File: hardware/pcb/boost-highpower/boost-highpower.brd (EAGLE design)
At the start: 41.1 x 22.3 mm, 28 parts

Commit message: moved some components
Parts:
- moved R11 50.8 mm to (41.9, 8.89)
- moved R15 50.8 mm to (27.9, 2.54), turned to 270 degrees
- moved U$9 39.9 mm to (48.3, 11.4), turned to 270 degrees
- moved C26 37.2 mm to (26.8, 4.70), turned to 180 degrees
- moved U$10 33.4 mm to (48.3, 17.8), turned to 270 degrees
- moved C14 31.9 mm to (41.9, 11.4)
- moved R12 30.2 mm to (41.9, 10.2)
- moved U$3 27.9 mm to (38.1, 19.1)
- moved X2 22.2 mm to (64.8, 15.2)
- moved C23 21.0 mm to (59.7, 10.2)
- moved R14 20.3 mm to (25.4, 2.54), turned to 270 degrees
- moved RSENSE 18.9 mm to (27.9, 16.5), turned to 90 degrees
- moved X1 17.3 mm to (12.7, 15.2)
- moved C28 13.5 mm to (17.8, 10.2)
- moved C24 12.6 mm to (54.6, 10.2)
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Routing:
- added copper zone on layer 16, net GND
- added copper zone on layer 1, net VIN
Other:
- board size 41.1 x 22.3 mm -> 94.5 x 38.8 mm

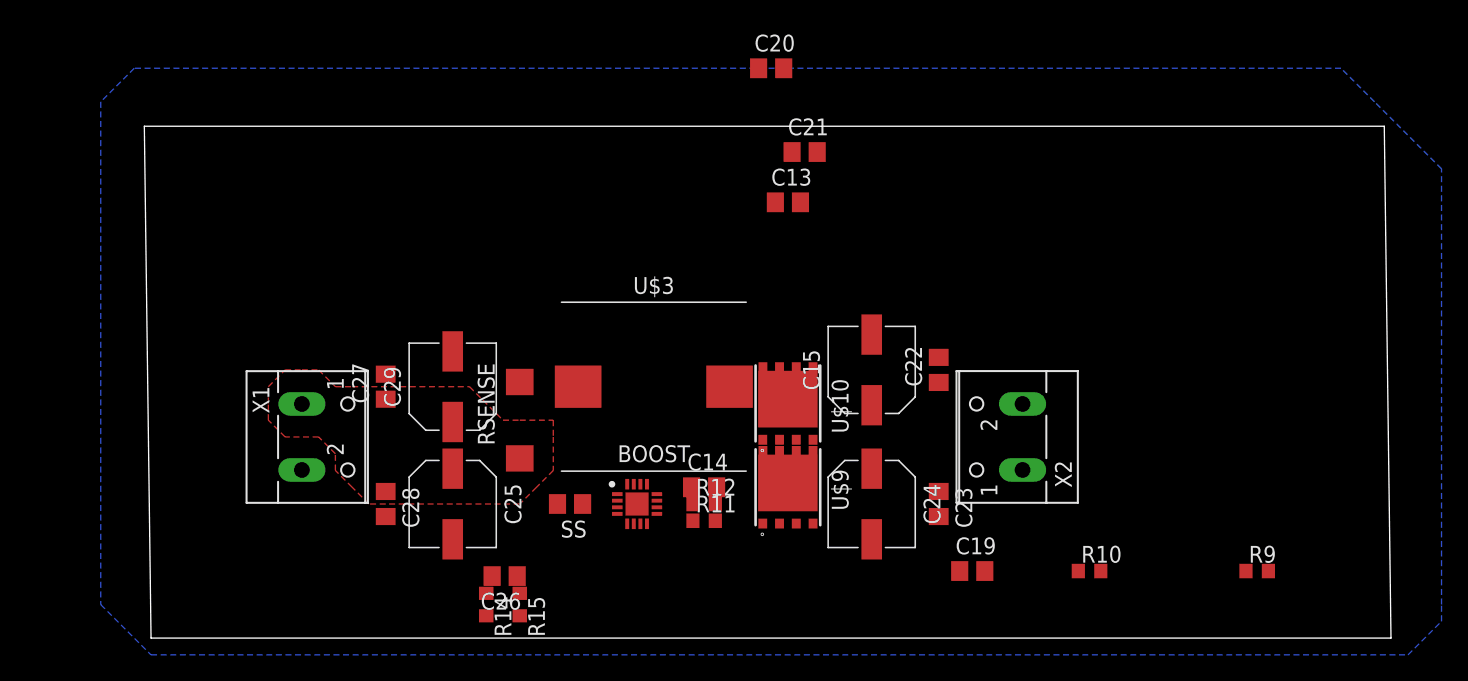
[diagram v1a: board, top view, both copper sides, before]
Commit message: Moved components to a first place
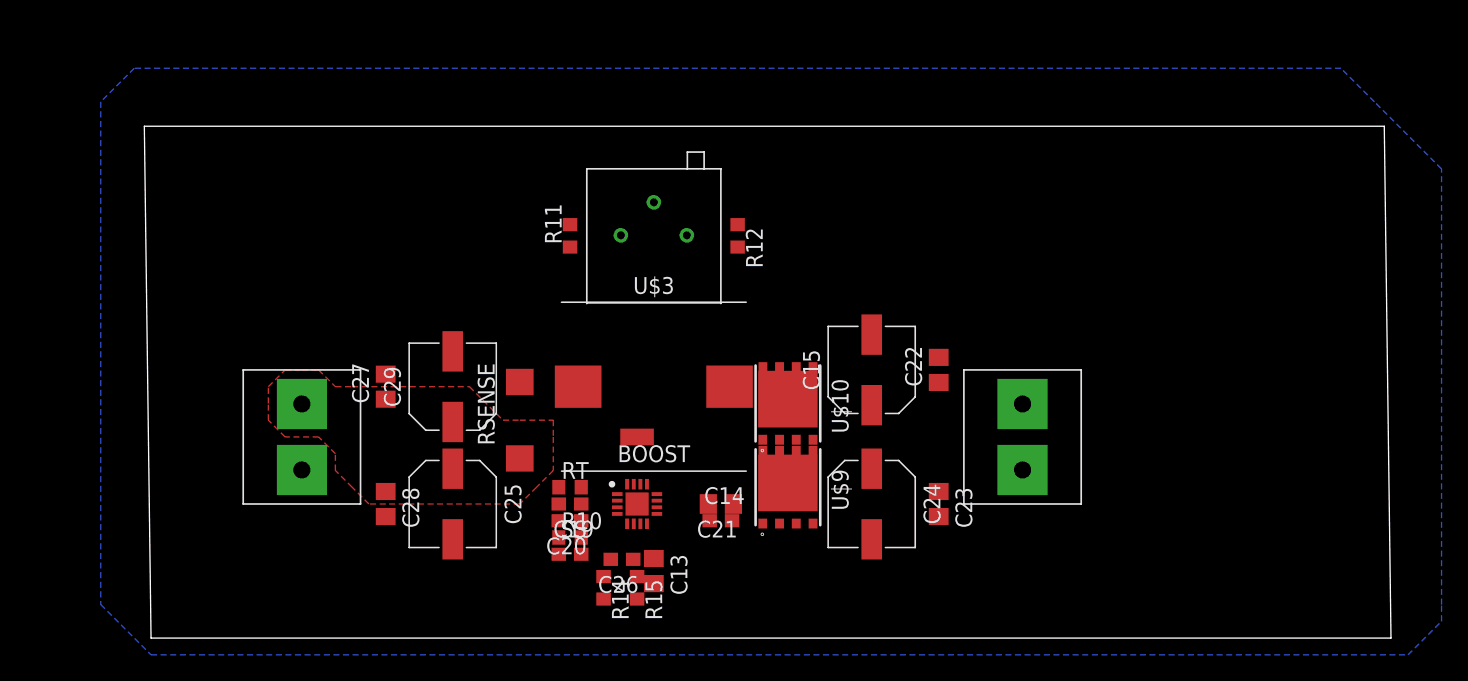
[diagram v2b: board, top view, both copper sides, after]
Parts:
- removed R9: 75k, rcl:R0603
- removed X1, X2: (no value), con-wago-500:W237-102
- added RT: 75k, rcl:R0603
- added U$1: SPLITTER, PowerManagement:SPLITTER
- added U$2: 67PR10KLF, Passive:67PR10KLF
- added U$4, U$5: TERMINAL_BLOCK_5MM_WPADS, Connectors:TERMINAL_5MM_WITH_SOLDERPADS
- C14: value 4.7µF -> 1µF; device rcl:C0805 -> rcl:C0603
- C19, C20, C26, SS: device rcl:C0805 -> rcl:C0603
- C21: value 100nF -> 0.1µF
- R11: value 10k -> 1k
- R12: value 88k -> 34.1k
- moved R10 39.5 mm to (31.8, 7.62)
- moved C20 37.5 mm to (31.8, 8.89), turned to 180 degrees
- moved C19 30.5 mm to (31.8, 6.35)
- moved C13 29.7 mm to (38.1, 5.08), turned to 270 degrees
- moved C21 27.4 mm to (43.2, 10.2), turned to 180 degrees
- moved R11 23.9 mm to (31.8, 30.5), turned to 90 degrees
- moved R12 20.5 mm to (44.5, 30.5), turned to 270 degrees
- moved R14 8.98 mm to (34.3, 3.81)
- moved C26 8.98 mm to (35.7, 5.97)
- moved R15 8.98 mm to (36.8, 3.81)
- moved C14 2.84 mm to (43.2, 8.89)
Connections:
- net N$12 renamed SS
- net N$16 renamed BOOT
- net N$19 renamed SW
- net N$2 renamed VCC
- net N$22 renamed ISNS-
- net N$23 renamed ISNS+
- removed net N$11: BOOST.1, R9.2
- new net AGND: BOOST.16, U$1.P$2
- new net N$3: R12.1, U$2.P$3
- new net N$4: R11.2, U$2.P$1
- new net RT: BOOST.1, RT.2
- net GND: now also RT.1, U$1.P$1, U$4.P$1, U$5.P$2; no longer BOOST.16, R9.1, X1.2, X2.1
- net N$20: now also U$2.P$2; no longer R11.2, R12.1
- net VIN: now also U$5.P$1; no longer X1.1
- net VOUT: now also U$4.P$2; no longer X2.2

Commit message: Routed board
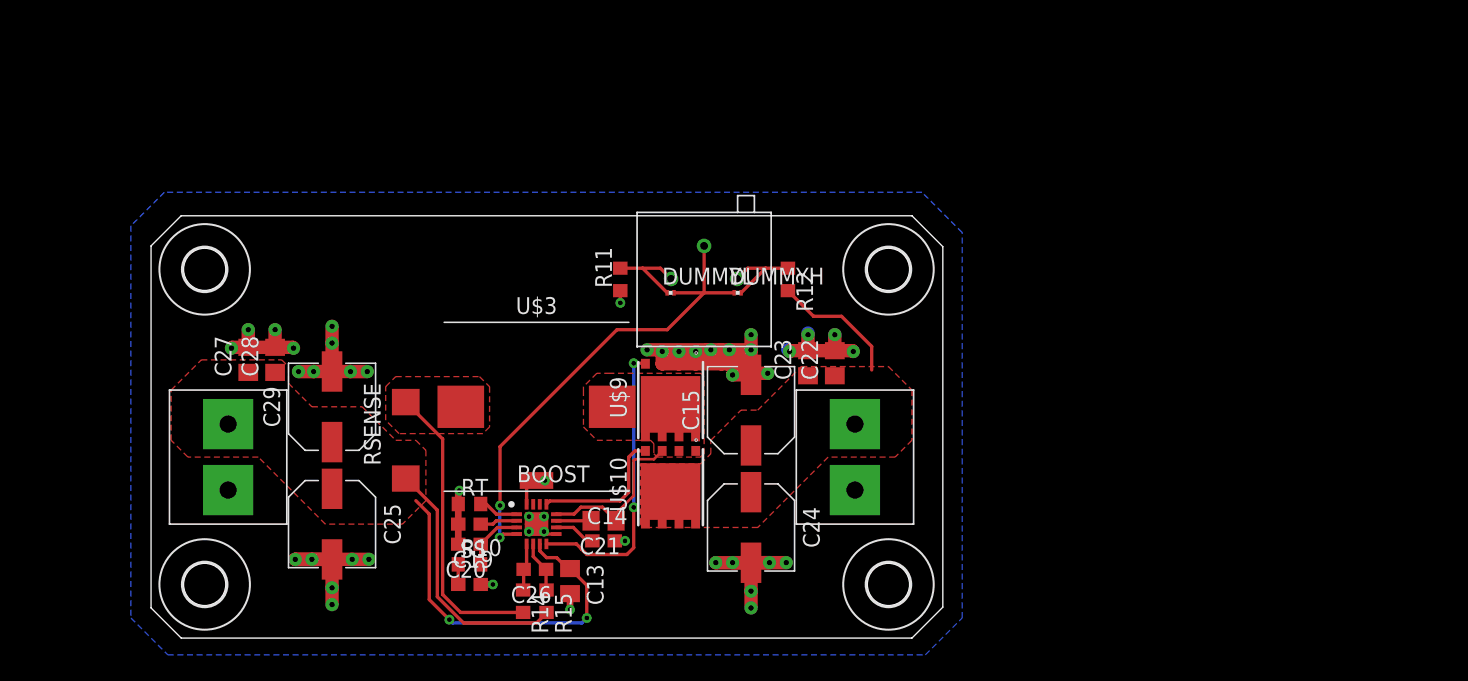
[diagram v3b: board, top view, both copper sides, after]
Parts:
- added DUMMYH, DUMMYL: (no value), rcl:R0201
- added H1, H2, H3, H4: MOUNT-HOLE3.2, holes:3,2
- moved C23 14.6 mm to (49.8, 20.8), turned to 90 degrees
- moved C28 13.8 mm to (9.40, 21.1), turned to 90 degrees
- moved U$4 12.8 mm to (53.3, 13.7)
- moved U$9 11.1 mm to (39.4, 18.0), turned to 90 degrees
- moved U$10 10.9 mm to (39.4, 11.4), turned to 90 degrees
- moved C27 10.6 mm to (7.37, 21.1)
- moved C15 9.64 mm to (45.5, 17.3)
- moved C24 9.32 mm to (45.5, 8.38)
- moved C25 9.27 mm to (13.7, 8.64)
- moved C29 9.27 mm to (13.7, 17.5)
- moved C14 9.02 mm to (34.3, 7.37)
- moved U$3 9.02 mm to (29.2, 17.5)
- moved C21 8.98 mm to (34.3, 8.89)
- moved RSENSE 8.77 mm to (19.3, 15.0)
- moved U$1 8.30 mm to (29.2, 11.9), turned to 270 degrees
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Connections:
- net N$20: now also DUMMYH.1, DUMMYL.2
- net N$3: now also DUMMYH.2
- net N$4: now also DUMMYL.1
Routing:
- net GND: track 0.00 -> 99.2 mm, vias 0 -> 46
- net VIN: track 0.00 -> 47.8 mm, vias 0 -> 2
- net N$20: track 0.00 -> 36.7 mm, vias 0 -> 2
- net N$18: track 0.00 -> 22.4 mm
- net LDRV: track 0.00 -> 22.1 mm, vias 0 -> 2
- net SW: track 0.00 -> 12.8 mm
- net HDRV: track 0.00 -> 10.7 mm
- net VOUT: track 0.00 -> 9.88 mm
- net N$3: track 0.00 -> 6.82 mm
- net N$4: track 0.00 -> 6.82 mm
- net COMP: track 0.00 -> 4.78 mm
- net ISNS+: track 0.00 -> 3.91 mm
- net ISNS-: track 0.00 -> 3.60 mm
- net VCC: track 0.00 -> 3.15 mm
- net RT: track 0.00 -> 3.05 mm
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- added copper zone on layer 1, net N$18
- added copper zone on layer 1, net SW
- added copper zone on layer 1, net VOUT
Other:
- board size 94.5 x 38.8 mm -> 60 x 32 mm
- board text added: "."
- board text added: "Boost module 4.5 - 35 V input 5 - 58 V output"
- board text added: "Boost module TSP43061 Oskar Johansson 2020-03-30 Rev 1"
- board text added: "Bridge if no pot"
- board text added: "GND"
- board text added: "VIN"

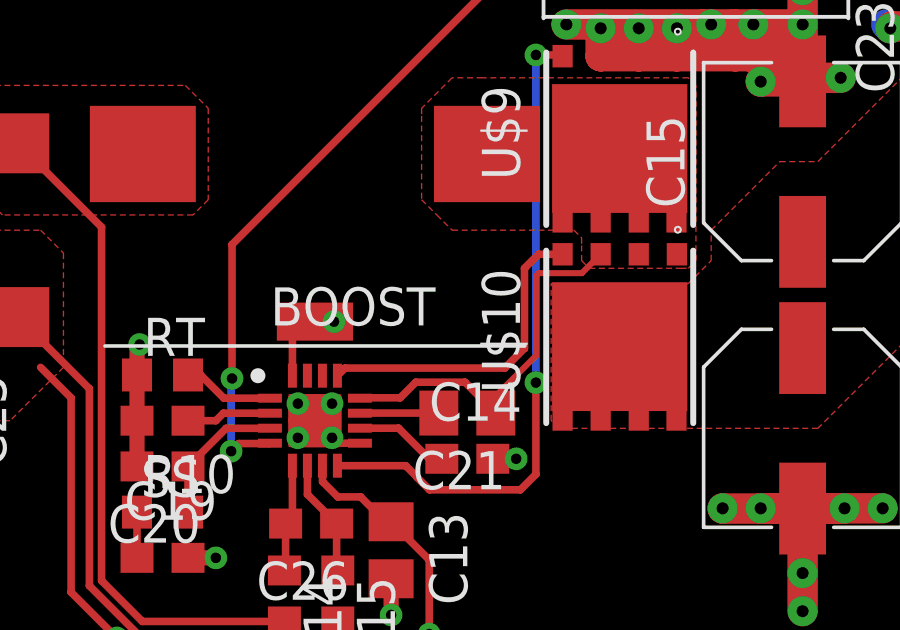
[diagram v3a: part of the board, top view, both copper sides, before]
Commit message: Added 10A to silkscreen
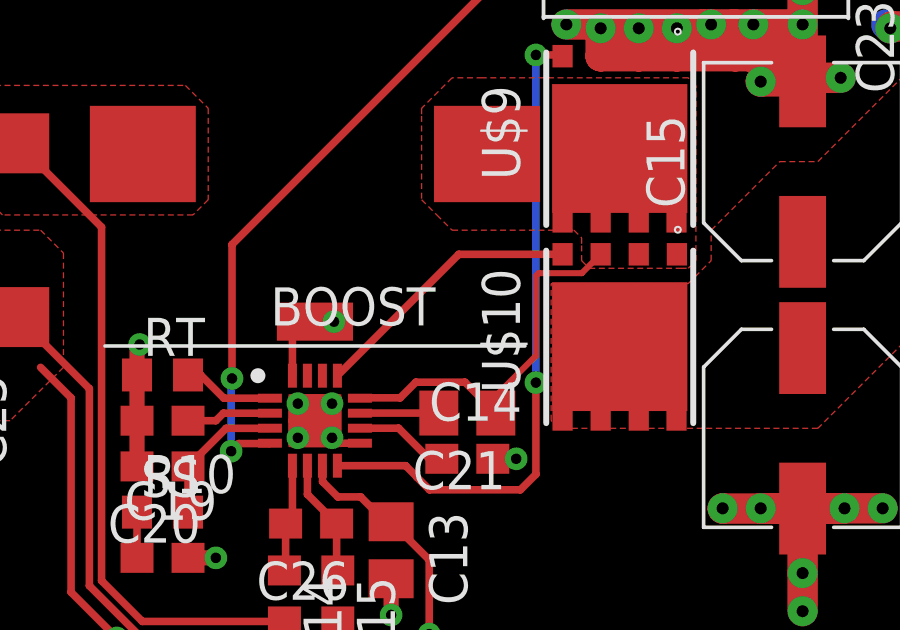
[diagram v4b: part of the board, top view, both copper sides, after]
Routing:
- net HDRV: track 10.7 -> 9.18 mm
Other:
- board text added: "Boost module 4.5 - 35 V input 5 - 58 V output 10 A"
- board text removed: "Boost module 4.5 - 35 V input 5 - 58 V output"
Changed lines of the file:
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@@
 <wire x1="0" y1="29.718" x2="0" y2="2.286" width="0" layer="20"/>
 <wire x1="0" y1="2.286" x2="2.286" y2="0" width="0" layer="20"/>
-<text x="10.16" y="29.972" size="1.2" layer="51" align="top-left">Boost module
+<text x="9.906" y="29.9974" size="1.2" layer="51" align="top-left">Boost module
 4.5 - 35 V input
- 5 - 58 V output</text>
+ 5 - 58 V output
+10 A</text>
 <text x="10.16" y="8.382" size="1.2" layer="51" align="top-right">GND</text>
 <text x="49.276" y="8.128" size="1.2" layer="51" align="top-left">GND</text>
@@
 <contactref element="BOOST" pad="13"/>
 <contactref element="U$10" pad="4"/>
-<wire x1="37.465" y1="14.1825" x2="36.6615" y2="14.1825" width="0.254" layer="1"/>
-<wire x1="35.536" y1="10.39" x2="30.214" y2="10.39" width="0.254" layer="1"/>
-<wire x1="30.214" y1="10.39" x2="29.96" y2="10.136" width="0.254" layer="1"/>
-<wire x1="36.6615" y1="14.1825" x2="36.195" y2="13.716" width="0.254" layer="1"/>
-<wire x1="36.195" y1="13.716" x2="36.195" y2="11.049" width="0.254" layer="1"/>
-<wire x1="36.195" y1="11.049" x2="35.536" y2="10.39" width="0.254" layer="1"/>
+<wire x1="37.465" y1="14.1825" x2="34.0065" y2="14.1825" width="0.254" layer="1"/>
+<wire x1="34.0065" y1="14.1825" x2="29.96" y2="10.136" width="0.254" layer="1"/>
 </signal>
 <signal name="VCC">

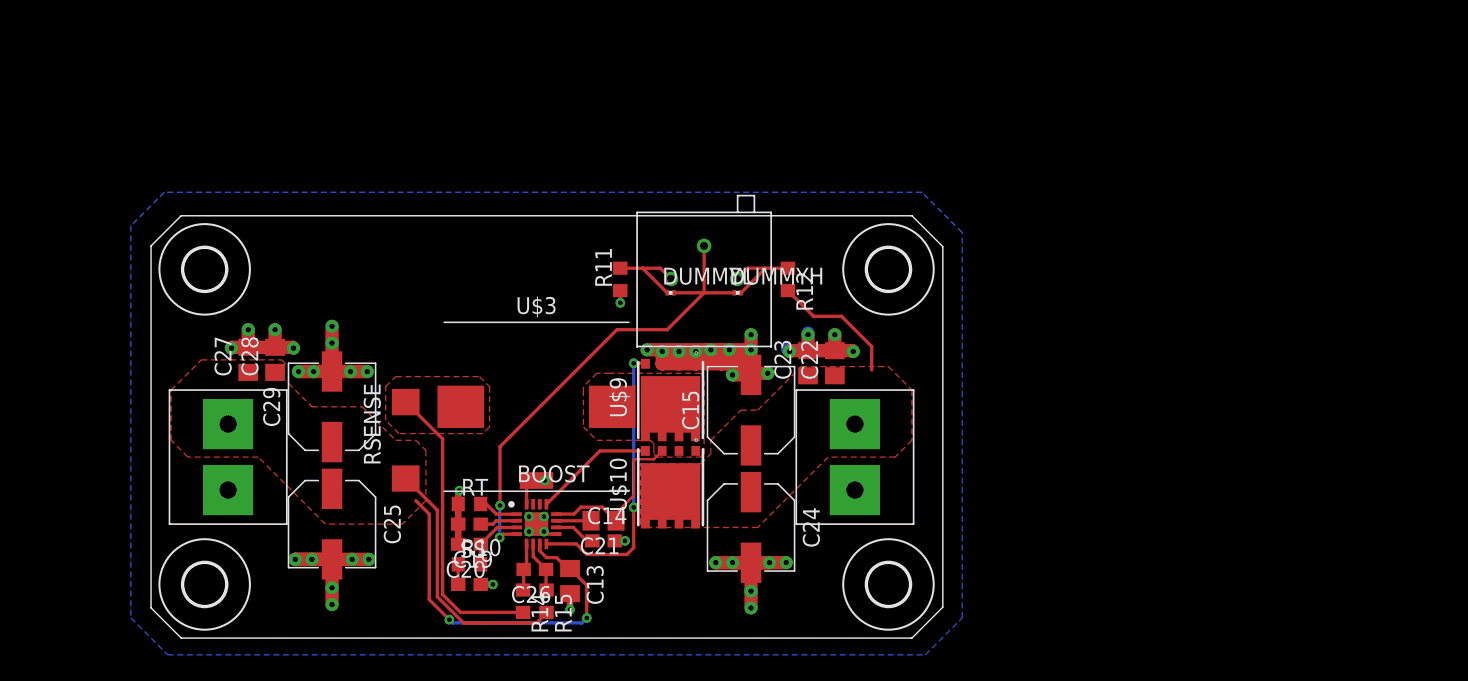
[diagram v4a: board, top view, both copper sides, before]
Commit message: Changed cap to 50V and 100V to meet requirement
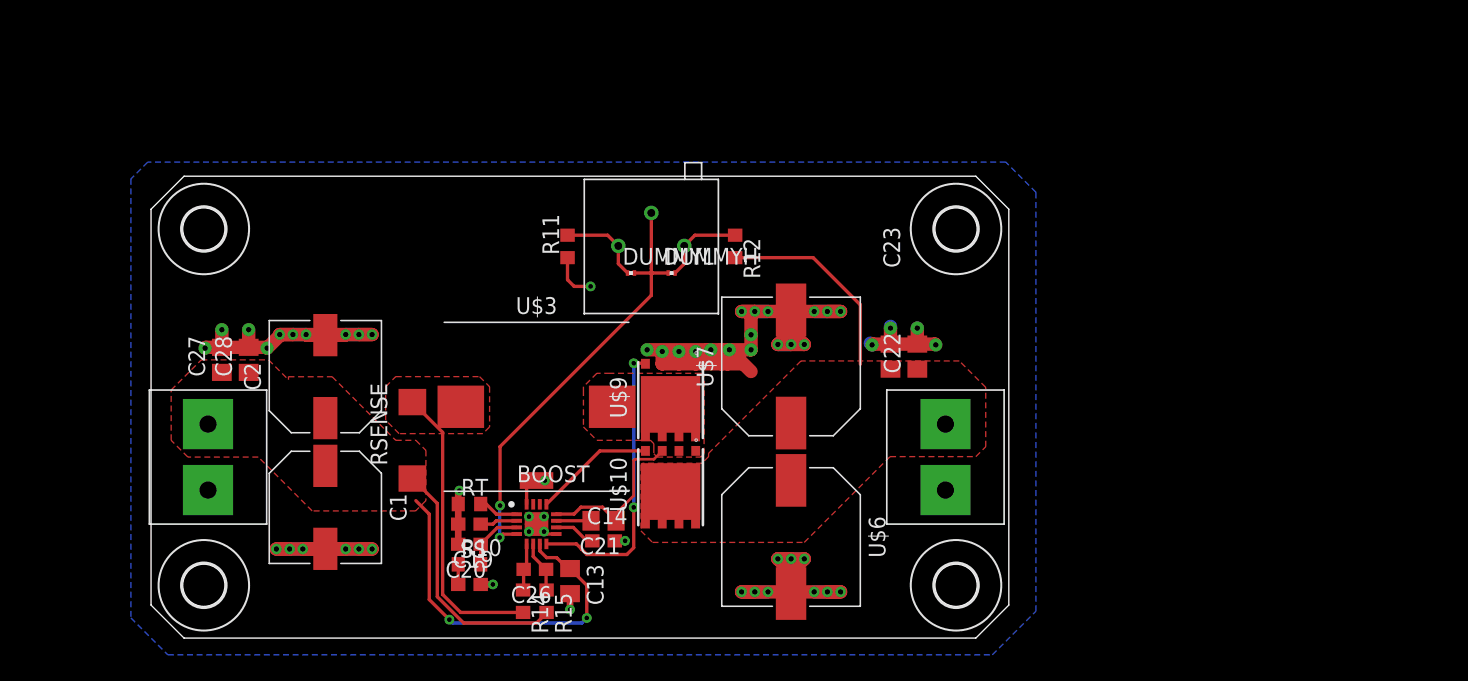
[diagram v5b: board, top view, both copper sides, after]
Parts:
- removed C15, C24, C25, C29: 100uF, Passive:CAPAE660X700N
- added C1, C2: 100µF, Passive:CAPAE830X850N
- added U$6, U$7: 100µF, Passive:CAPAE1030X1000N
- moved U$4 6.86 mm to (60.2, 13.7)
- moved C22 6.27 mm to (58.1, 21.3)
- moved C23 6.27 mm to (56.0, 21.3)
- moved H4 5.96 mm to (61.0, 31.0)
- moved DUMMYH 5.22 mm to (39.5, 27.7)
- moved H3 5.12 mm to (61.0, 4.00)
- moved R11 4.72 mm to (31.6, 29.7)
- moved U$2 4.72 mm to (37.9, 32.2)
- moved R12 4.72 mm to (44.3, 29.7)
- moved DUMMYL 3.35 mm to (36.4, 27.7)
- moved H1 3.06 mm to (4.00, 31.0)
- moved C27 2.00 mm to (5.37, 21.1)
- moved C28 2.00 mm to (7.40, 21.1)
- moved U$5 1.52 mm to (4.32, 13.7)
- moved RSENSE 0.50 mm to (19.8, 15.0)
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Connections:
- net GND: now also C1.2, C2.2, U$6.2, U$7.2; no longer C15.2, C24.2, C25.2, C29.2
- net VIN: now also C1.1, C2.1; no longer C25.1, C29.1
- net VOUT: now also U$6.1, U$7.1; no longer C15.1, C24.1
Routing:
- net GND: track 99.2 -> 139.8 mm, vias 46 -> 56
- net VOUT: track 9.88 -> 15.5 mm
- net N$20: track 36.7 -> 33.5 mm
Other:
- board size 60 x 32 mm -> 65 x 35 mm
- board text added: "Boost module TSP43061 Oskar Johansson 2020-03-31 Rev 2"
- board text added: "VOUT"
- board text removed: "Boost module TSP43061 Oskar Johansson 2020-03-30 Rev 1"
